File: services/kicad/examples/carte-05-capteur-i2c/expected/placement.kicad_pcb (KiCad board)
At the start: 2 copper layers, 70 x 50 mm, 26 parts, among them J1 IN_5V, J2 SWD, J3 I2C, U1 STM32F103C8T6, U2 AMS1117-3.3, U3 BME280

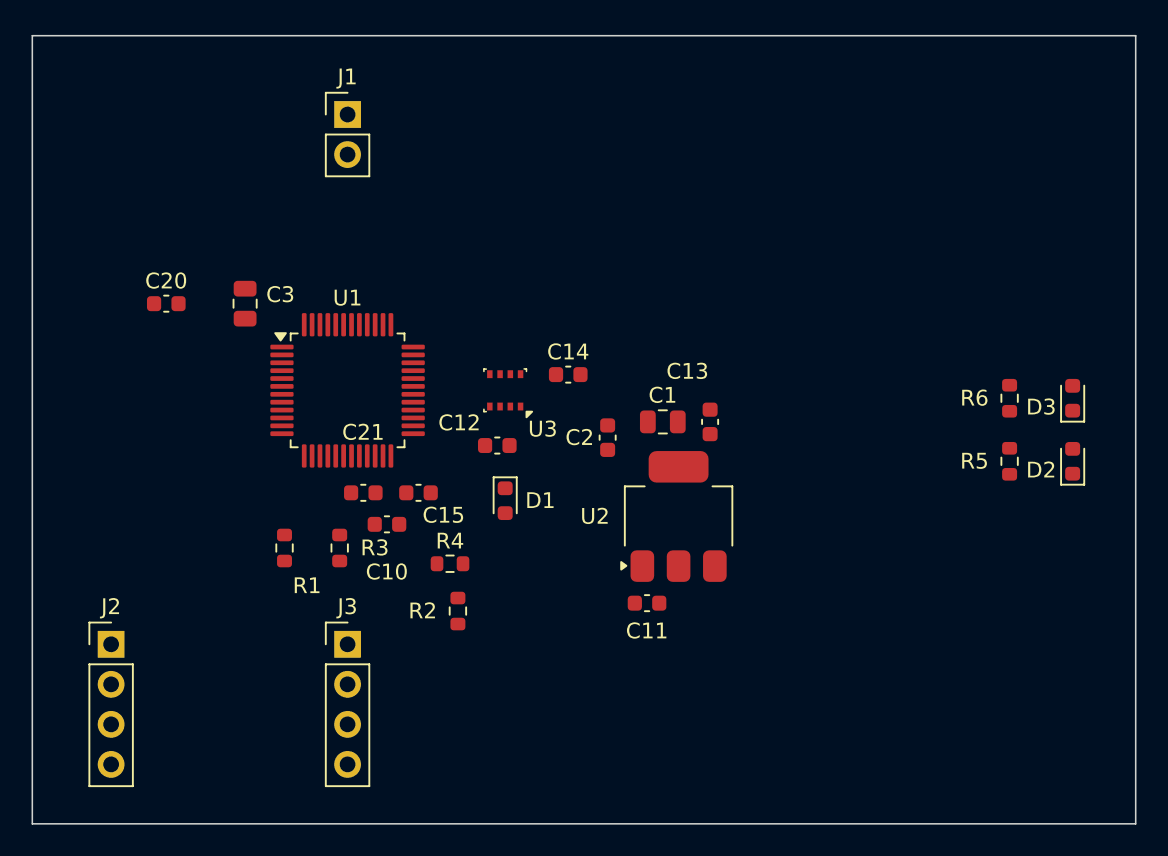
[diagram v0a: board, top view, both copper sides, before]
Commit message: chore(banc): relivrer carte-01/02/04/05 compactes (25 %, D-2026-09-20-a) (#222)
Chaine place -> route rejouee par HTTP sur les dix cartes avec le code de
#220/#221. Quatre sortent a 0 erreur et 0 connexion manquante, sur des
cartes 18 a 58 % plus petites :

  carte-01  24,8x17 -> 20x14      carte-02  55x40 -> 35x25
  carte-04  45x44,8 -> 39x30      carte-05  70x50 -> 46x33

placement.kicad_pcb et final.kicad_pcb remplaces ENSEMBLE ; mesures.json :
board recompte, drc_du_board rejuge (remesurer_banc.py), cle
carte_compacte (tailles et vias d avant, durees, moteur, pistes par
couche). Rendus refaits. Connecteurs a <= 5 mm d un bord (carte-02 J2 :
13,9 -> 3,8 mm) ; carte-05 J3 inchange a 11,4 mm (origine pin 1).

Les six autres gardent leur board du 2026-09-19 : 06 et 08 a 1 manquante,
03 et 07 mauvais, 09 et 10 sans board (tirages figes). Detail dans
BANC_DRIVER_LLM.md. carte-11 non touchee.


Claude-Session: https://claude.ai/code/session_01TnMqm4La2CxQHHB5K8aSSV

Co-authored-by: Claude Fable 5.1 <noreply@anthropic.com>
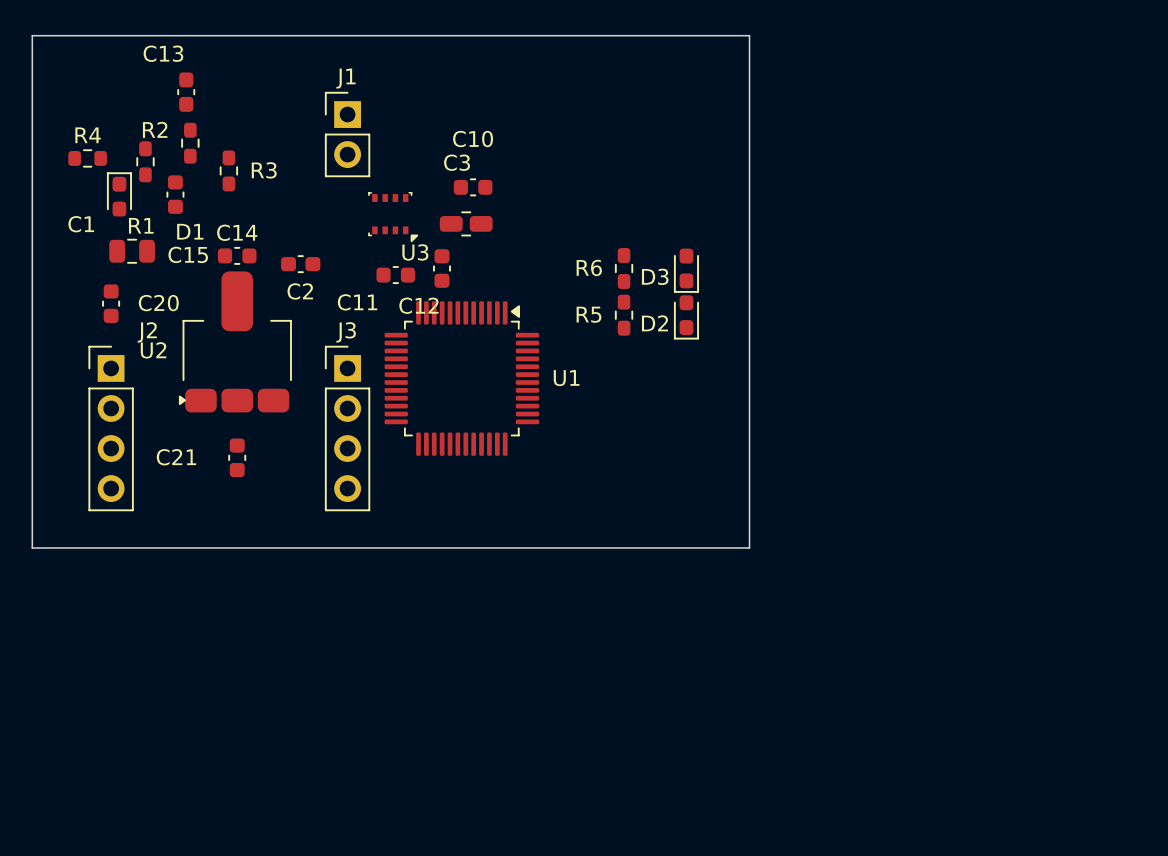
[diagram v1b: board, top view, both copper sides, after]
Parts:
- moved C13 39.3 mm to (123.3, 83.6)
- moved C1 35.4 mm to (119.8, 93.7)
- moved R4 34.5 mm to (117.0, 87.8)
- moved R2 34.2 mm to (123.5, 86.8)
- moved D1 31.2 mm to (119.0, 90.2)
- moved U2 29.9 mm to (126.5, 100.0)
- moved C11 26.2 mm to (136.6, 95.2)
- moved D2 26.2 mm to (155.0, 97.7)
- moved R5 26.2 mm to (151.0, 97.7)
- moved R1 26.0 mm to (120.7, 88.0)
- moved D3 25.8 mm to (155.0, 94.8)
- moved R6 25.8 mm to (151.0, 94.8)
- moved R3 24.9 mm to (126.0, 88.6)
- moved C15 24.4 mm to (122.6, 90.1), turned to 90 degrees
- moved C2 22.4 mm to (130.5, 94.5), turned to 0 degrees
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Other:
- board size 70 x 50 mm -> 45.5 x 32.5 mm

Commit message: fix(kicad): plan de masse referme — banc DIX cartes sur dix, 0 erreur 0 manquante (#237)
* docs(kicad): la derniere rupture de plan tient a UN segment, pas a un faisceau

Diagnostic complet du seul defaut restant du banc (carte-10), mesure sur le
board qui le porte vraiment, apres consultation de Codex et de GLM.

Mesures sur `/tmp/livr/carte-10-maximale/route.kicad_pcb` (33 violations,
0 erreur, 1 connexion manquante) :

- 23 ilots GND sur les deux faces, exactement 2 orphelins, et ce sont des
  JUMEAUX : F.Cu 1,30 mm2 (porte la pastille C35.2) et B.Cu 0,99 mm2.
- AUCUN de leurs points n a le plan principal en vis-a-vis : ils se font face
  l un l autre. La piste « changer de face par un via », proposee par GLM, est
  donc REFUTEE par la mesure.
- La couture de production visite les deux ilots et refuse la totalite de
  leurs sites (23 et 18 candidats ; obstacle 16/10, hors_polygone 6/7,
  trou_trop_pres 1/1) : un via ne tient pas dans un millimetre carre.
  Le raccord par courte piste rend relies 0, sans_chemin 19.
- Mais le plan principal n est qu a 0,862 mm sur F.Cu et 0,781 mm sur B.Cu, et
  UN SEUL segment coupe le couloir de chaque face (EXT2_1, EXT4_1).

Le plan de Codex — deplacer l obstacle au lieu de chercher un passage a
travers — a donc ici un ensemble a arracher d UN segment par face, pas une
recherche ouverte. Decision de strategie de routage : D-2026-09-22-a, EN
ATTENTE. Rien n est implemente.

Levier natif verifie et jamais appele : LocalRerouter.reroute_segment() de
kicad-tools, utilise par drc/repair_clearance.py, zero appelant Cirqix. Il
travaille sur le document S-expression quand notre code travaille sur pcbnew.

Lecons inscrites dans CLAUDE.md :
- j ai d abord mesure le board VERSIONNE du 21, qui est propre (non_connectes
  0) et se pretait a toutes les demonstrations — un via y tenait avec 0,29 mm
  de marge. Verifier que l artefact PORTE le defaut avant de le diagnostiquer.
- ma premiere sonde raisonnait zone par zone, alors que la carte por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
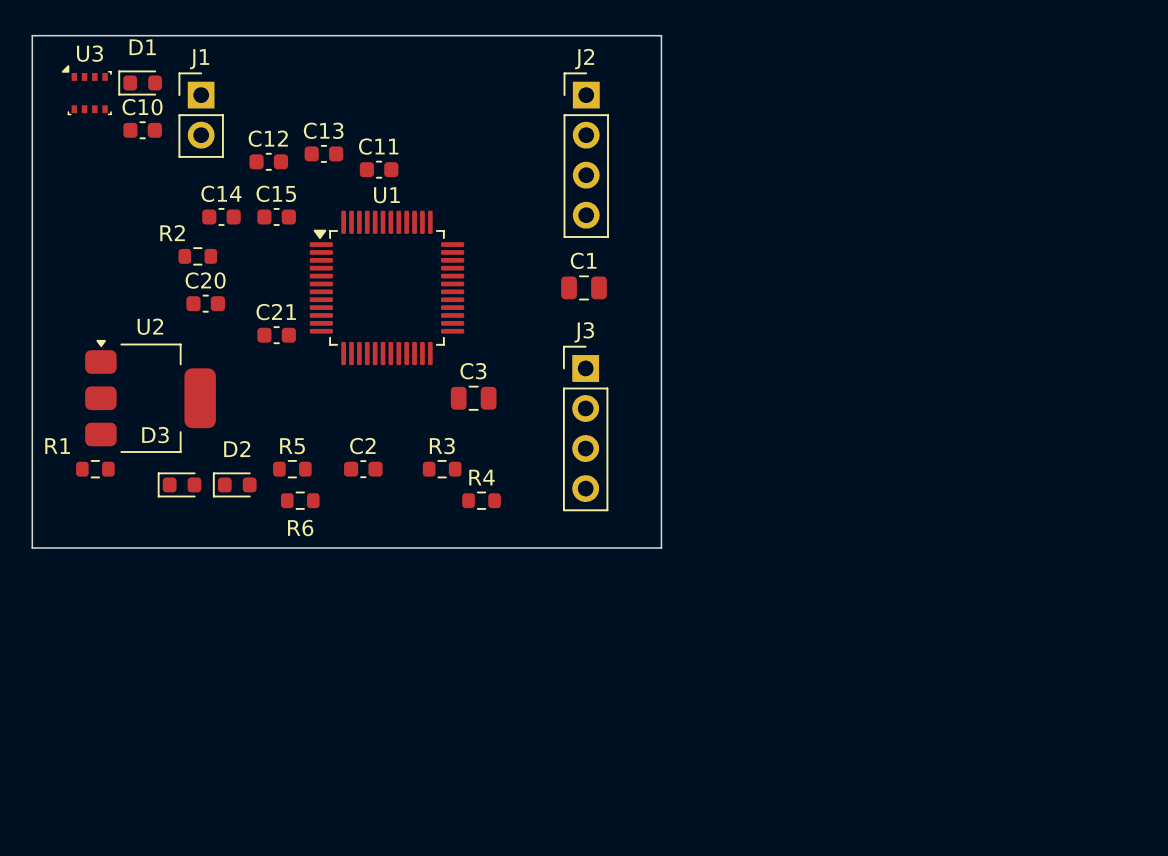
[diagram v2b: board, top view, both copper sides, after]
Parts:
- moved D3 34.8 mm to (123.0, 108.5), turned to 0 degrees
- moved J2 34.8 mm to (148.6, 83.8)
- moved R4 33.1 mm to (142.0, 109.5)
- moved D2 30.5 mm to (126.5, 108.5), turned to 0 degrees
- moved C1 28.8 mm to (148.5, 96.0)
- moved R6 25.3 mm to (130.5, 109.5), turned to 0 degrees
- moved R3 23.3 mm to (139.5, 107.5), turned to 0 degrees
- moved R5 23.2 mm to (130.0, 107.5), turned to 0 degrees
- moved C10 21.3 mm to (120.5, 86.0)
- moved U3 20.6 mm to (117.1, 83.6), turned to 0 degrees
- moved R1 19.8 mm to (117.5, 107.5), turned to 0 degrees
- moved J3 15.1 mm to (148.6, 101.1)
- moved C2 13.6 mm to (134.5, 107.5)
- moved C12 12.9 mm to (128.5, 88.0), turned to 0 degrees
- moved C3 11.1 mm to (141.5, 103.0)
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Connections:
- U1 pad 36: Net-(U1-36) -> PWR_FLAG
- U1 pad 48: Net-(U1-48) -> PWR_FLAG
- U1 pad 9: Net-(U1-9) -> PWR_FLAG
- U2 pad 3: VIN -> PWR_FLAG
- U3 pad 6: SDA -> PWR_FLAG
- U3 pad 7: Net-(U3-7) -> PWR_FLAG
- U3 pad 8: Net-(U3-8) -> PWR_FLAG
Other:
- board size 45.5 x 32.5 mm -> 39.9 x 32.5 mm

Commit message: fix(banc): le banc route comme la production — plafond 8, budget du client
D-2026-09-24-f. run_pipeline.py prenait 2 couches et 1800 s par défaut, et
carte-07 écrivait 2 en dur : dix cartes sur quinze ne pouvaient jamais
escalader, et la règle « toute connexion manquante fait monter » était
inerte dans le banc. Mesuré sur carte-07 : 97 %, seule la masse manquante,
« le palier suivant sera tenté »… puis retour à 2 couches.

Plafond par défaut 8 (client Pro Max), budget min(600 + 300 x plafond, 3600)
comme routingSearchBudgetS côté client. En production, rien ne change : le
plafond reste celui du plan.

Livraisons du jour, toutes vérifiées par kicad-cli et contre le schéma
(0 erreur bloquante, 0 connexion manquante, 0 court-circuit) :
carte-04, 05, 06, 08 (campagne de l'après-midi) et carte-09, 10 (4 couches).
Les boards versionnés de ces cartes court-circuitaient des nets du schéma.

Correction de ma propre erreur dans la doc : carte-07 n'avait jamais
escaladé ; les lignes « palier 4 et 6 » du journal étaient celles de
carte-08, démarrée la même minute.

Co-Authored-By: Claude Opus 5.5 <noreply@anthropic.com>
Claude-Session: https://claude.ai/code/session_01TnMqm4La2CxQHHB5K8aSSV
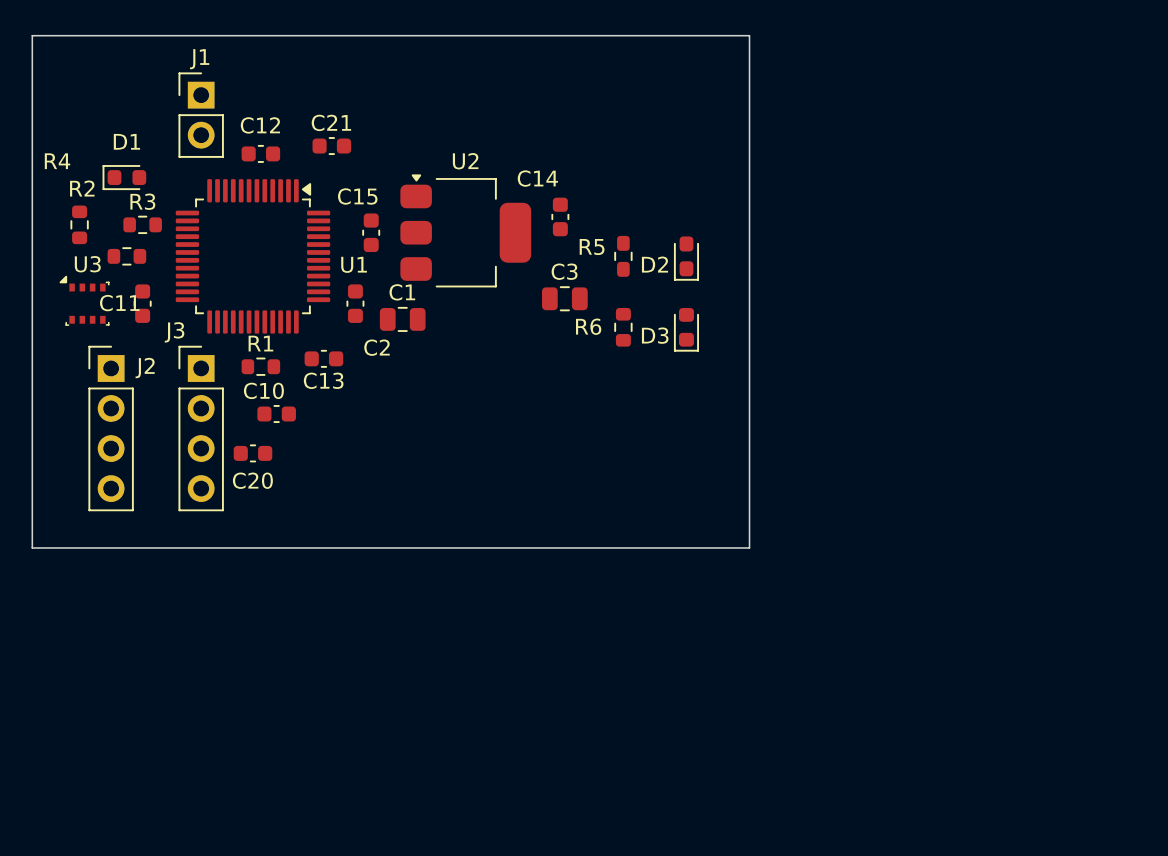
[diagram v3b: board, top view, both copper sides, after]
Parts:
- moved J2 34.8 mm to (118.5, 101.1)
- moved D3 33.5 mm to (155.0, 98.5), turned to 90 degrees
- moved D2 32.0 mm to (155.0, 94.0), turned to 90 degrees
- moved R4 30.9 mm to (116.5, 92.0), turned to 90 degrees
- moved R5 25.0 mm to (151.0, 94.0), turned to 90 degrees
- moved R3 24.5 mm to (120.5, 92.0)
- moved J3 24.4 mm to (124.2, 101.1)
- moved R6 23.3 mm to (151.0, 98.5), turned to 90 degrees
- moved U2 22.6 mm to (141.0, 92.5)
- moved C14 21.5 mm to (147.0, 91.5), turned to 90 degrees
- moved C10 19.9 mm to (129.0, 104.0)
- moved C11 17.2 mm to (120.5, 97.0), turned to 90 degrees
- moved U3 13.4 mm to (117.0, 97.0)
- moved C13 13.0 mm to (132.0, 100.5), turned to 180 degrees
- moved C21 12.5 mm to (132.5, 87.0)
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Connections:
- U1 pad 36: PWR_FLAG -> +3V3
- U1 pad 48: PWR_FLAG -> +3V3
- U1 pad 9: PWR_FLAG -> Net-(U1-9)
- U2 pad 3: PWR_FLAG -> VIN
- U3 pad 6: PWR_FLAG -> SDA
- U3 pad 7: PWR_FLAG -> GND
- U3 pad 8: PWR_FLAG -> Net-(U3-8)
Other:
- board size 39.9 x 32.5 mm -> 45.5 x 32.5 mm
